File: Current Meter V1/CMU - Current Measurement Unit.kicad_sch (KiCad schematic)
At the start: 35 parts, among them J1 USB_C_Receptacle_PowerOnly_6P, J102 I2C OLED Display Connector, U1 AMS1117-3.3, U101 STM32L432KCUx, U104 A1308xLHxx-1, U105 MCP6002-xSN

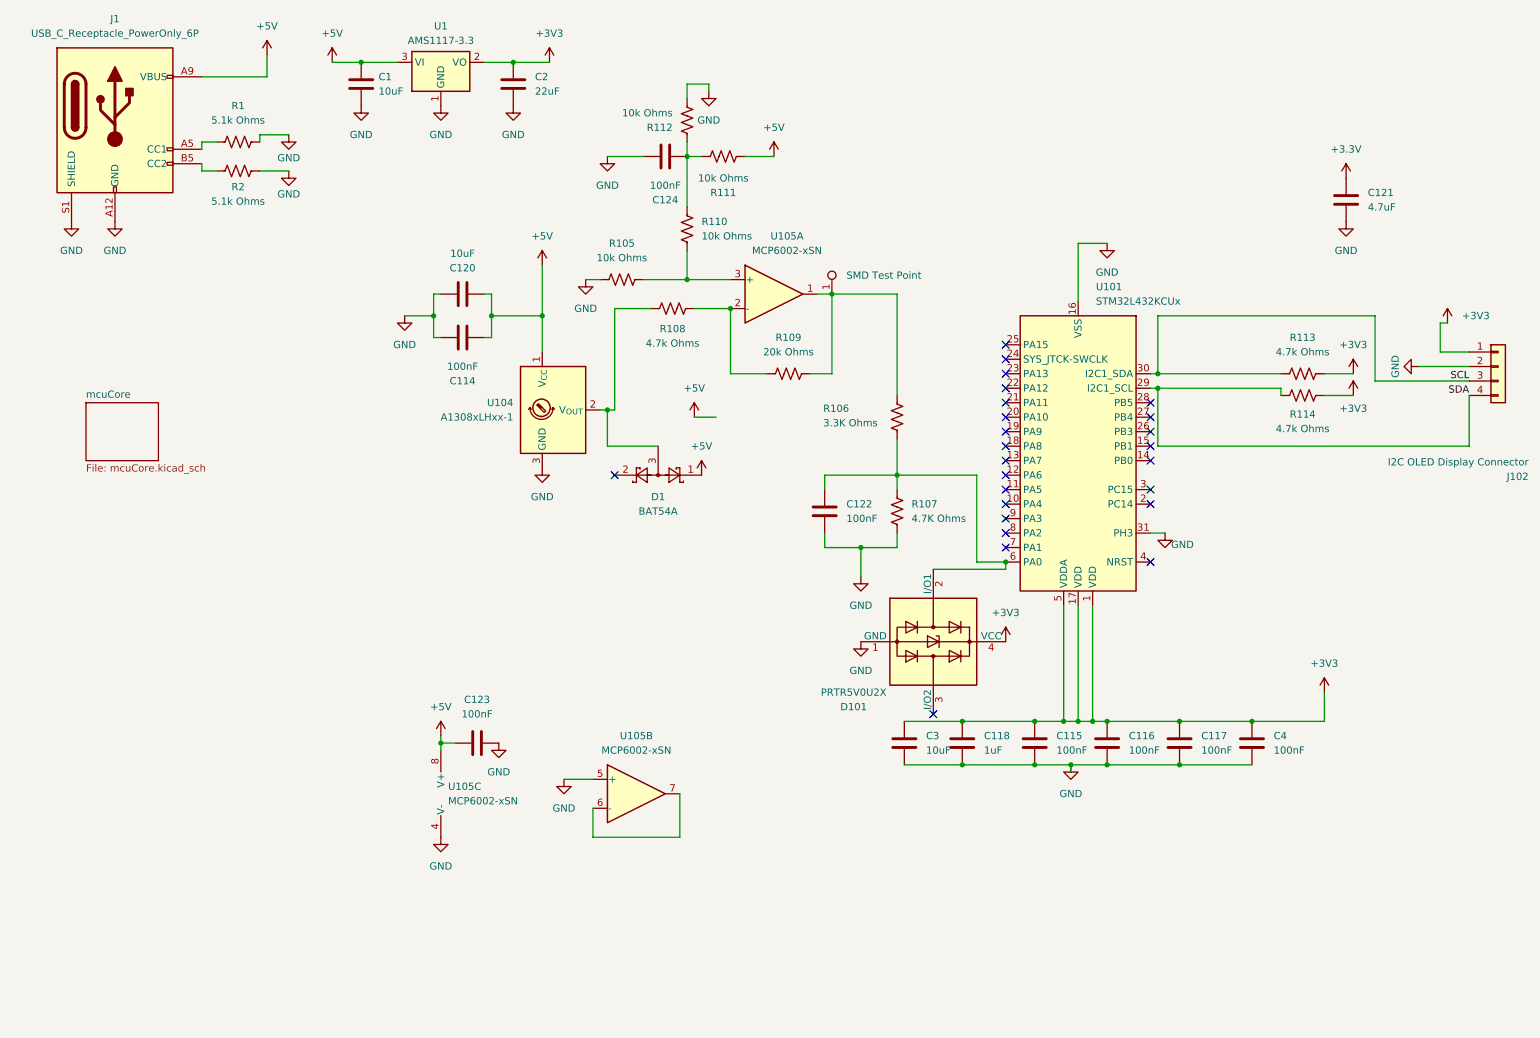
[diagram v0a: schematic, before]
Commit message: sheet organization and microcontroller updated
organized schematic into hierarchical sheets and updated pins on microcontroller
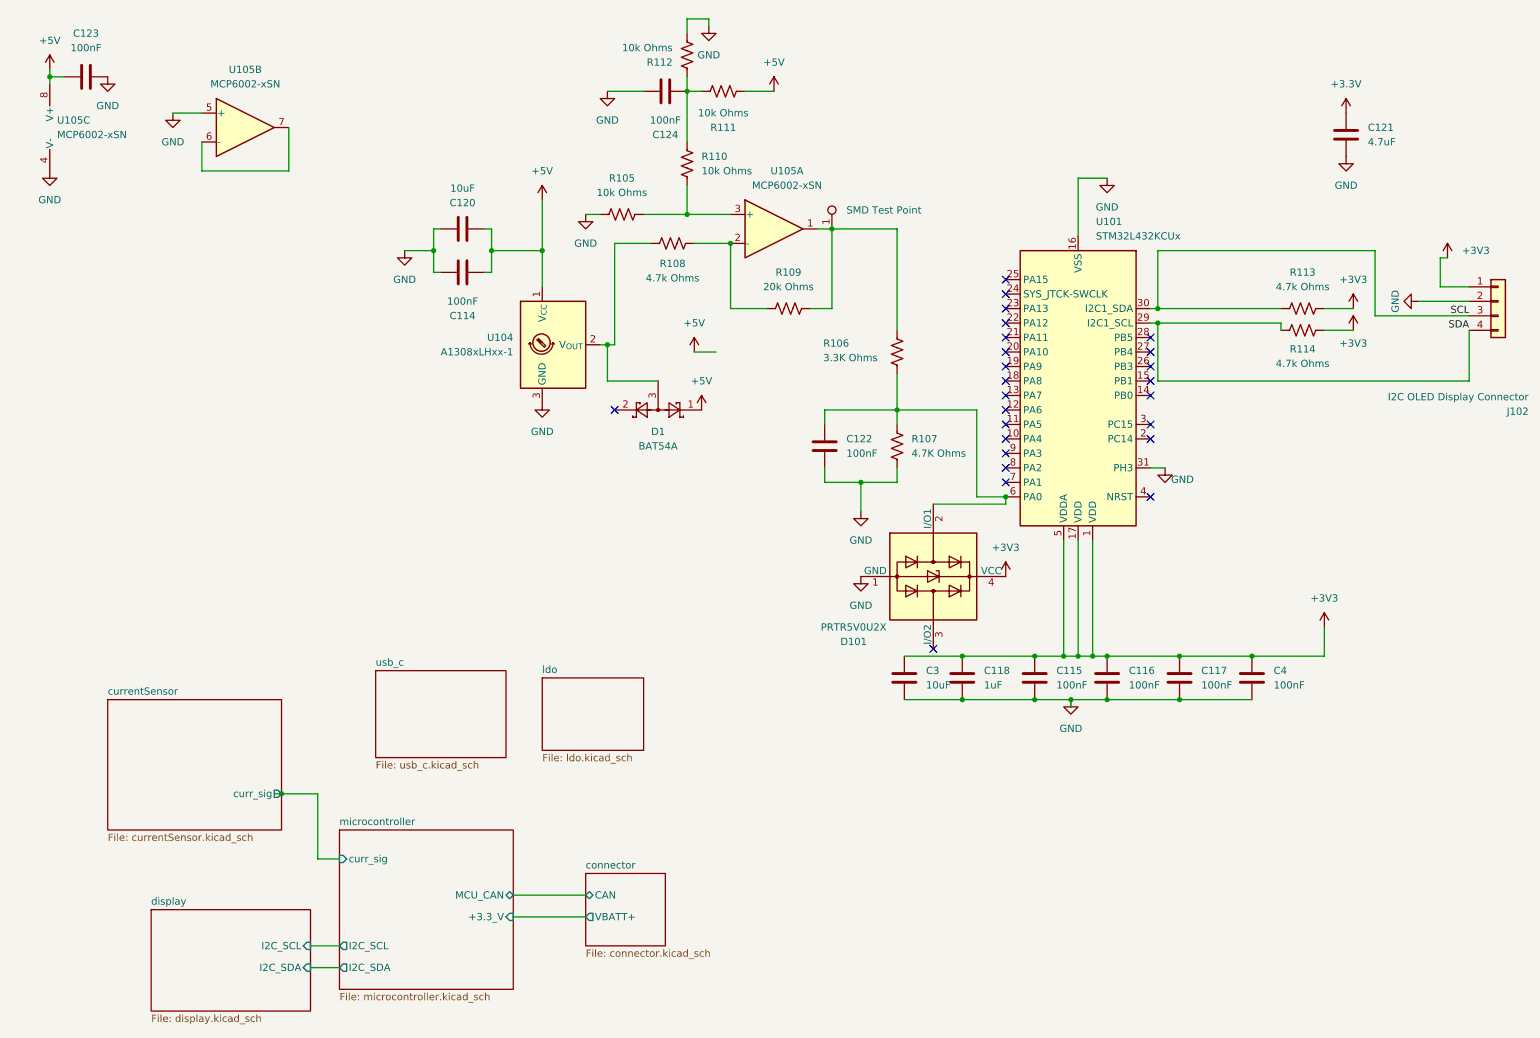
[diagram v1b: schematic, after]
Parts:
- removed C1: 10uF, symbol Device:C
- removed C2: 22uF, symbol Device:C
- removed J1: USB_C_Receptacle_PowerOnly_6P, symbol Connector:USB_C_Receptacle_PowerOnly_6P
- removed R1, R2: 5.1k Ohms, symbol Device:R_US
- removed U1: AMS1117-3.3, Package_TO_SOT_SMD:SOT-223-3_TabPin2, symbol Regulator_Linear:AMS1117-3.3
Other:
- removed sheet mcuCore
- added sheet connector (connector.kicad_sch)
- added sheet currentSensor (currentSensor.kicad_sch)
- added sheet display (display.kicad_sch)
- added sheet ldo (ldo.kicad_sch)
- added sheet microcontroller (microcontroller.kicad_sch)
- added sheet usb_c (usb_c.kicad_sch)
- moved on the sheet: C114, C115, C116, C117, C118, C120, C121, C122, C123, C124, C3, C4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

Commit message: microcontroller
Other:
- sheet ldo renamed NOTUSED_ldo
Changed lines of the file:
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@@
 	)
 	(sheet
-		(at 105.41 130.81)
+		(at 38.1 72.39)
 		(size 17.78 12.7)
 		(exclude_from_sim no)
@@
 			(color 0 0 0 0.0000)
 		)
-		(property "Sheetname" "ldo"
-			(at 105.41 130.0984 0)
+		(property "Sheetname" "NOTUSED_ldo"
+			(at 38.1 71.6784 0)
 			(effects
 				(font
@@
 		)
 		(property "Sheetfile" "ldo.kicad_sch"
-			(at 105.41 144.0946 0)
+			(at 38.1 85.6746 0)
 			(effects
 				(font
@@
 		)
 		(property "Field2" ""
-			(at 105.41 130.81 0)
+			(at 38.1 72.39 0)
 			(effects
 				(font

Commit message: microcontroller update
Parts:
- renumbered C123 to C101, C120 to C102, C114 to C103, C124 to C104, C122 to C105, C3 to C106, C118 to C107, C115 to C108, C116 to C109, C117 to C110, C4 to C111, C121 to C112, D1 to D101, D101 to D102, J102 to J101, R105 to R101, R108 to R102, R112 to R103, R110 to R104, R111 to R105, R109 to R106, R106 to R107, R107 to R108, R113 to R109, R114 to R110, U105 to U101, U104 to U102, U101 to U103
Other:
- sheet currentSensor renamed OLD_currentSensor
- added sheet opamp (opamp.kicad_sch)
- sheet OLD_currentSensor ports: added none; removed curr_sig
- sheet connector ports: added +5_V; removed VBATT+
- sheet microcontroller ports: added +5_V; removed +3.3_V
